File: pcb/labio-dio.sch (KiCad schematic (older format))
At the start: 98 parts

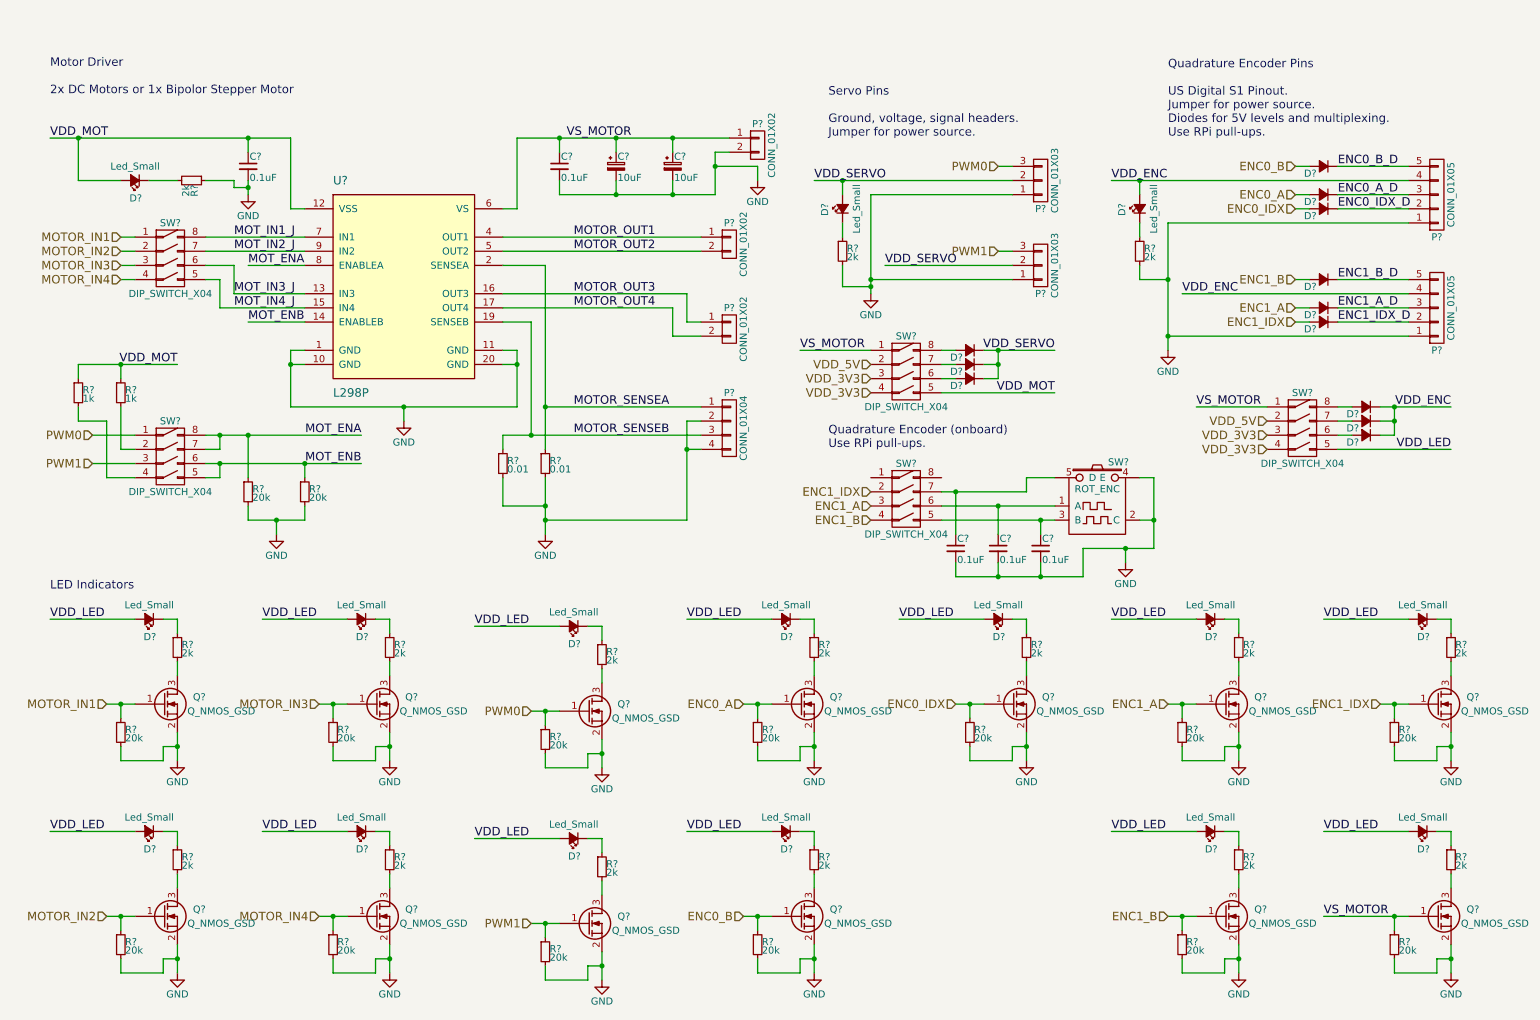
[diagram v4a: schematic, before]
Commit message: make extra footprints. start floorplan. fix display nets. add power expansion header.
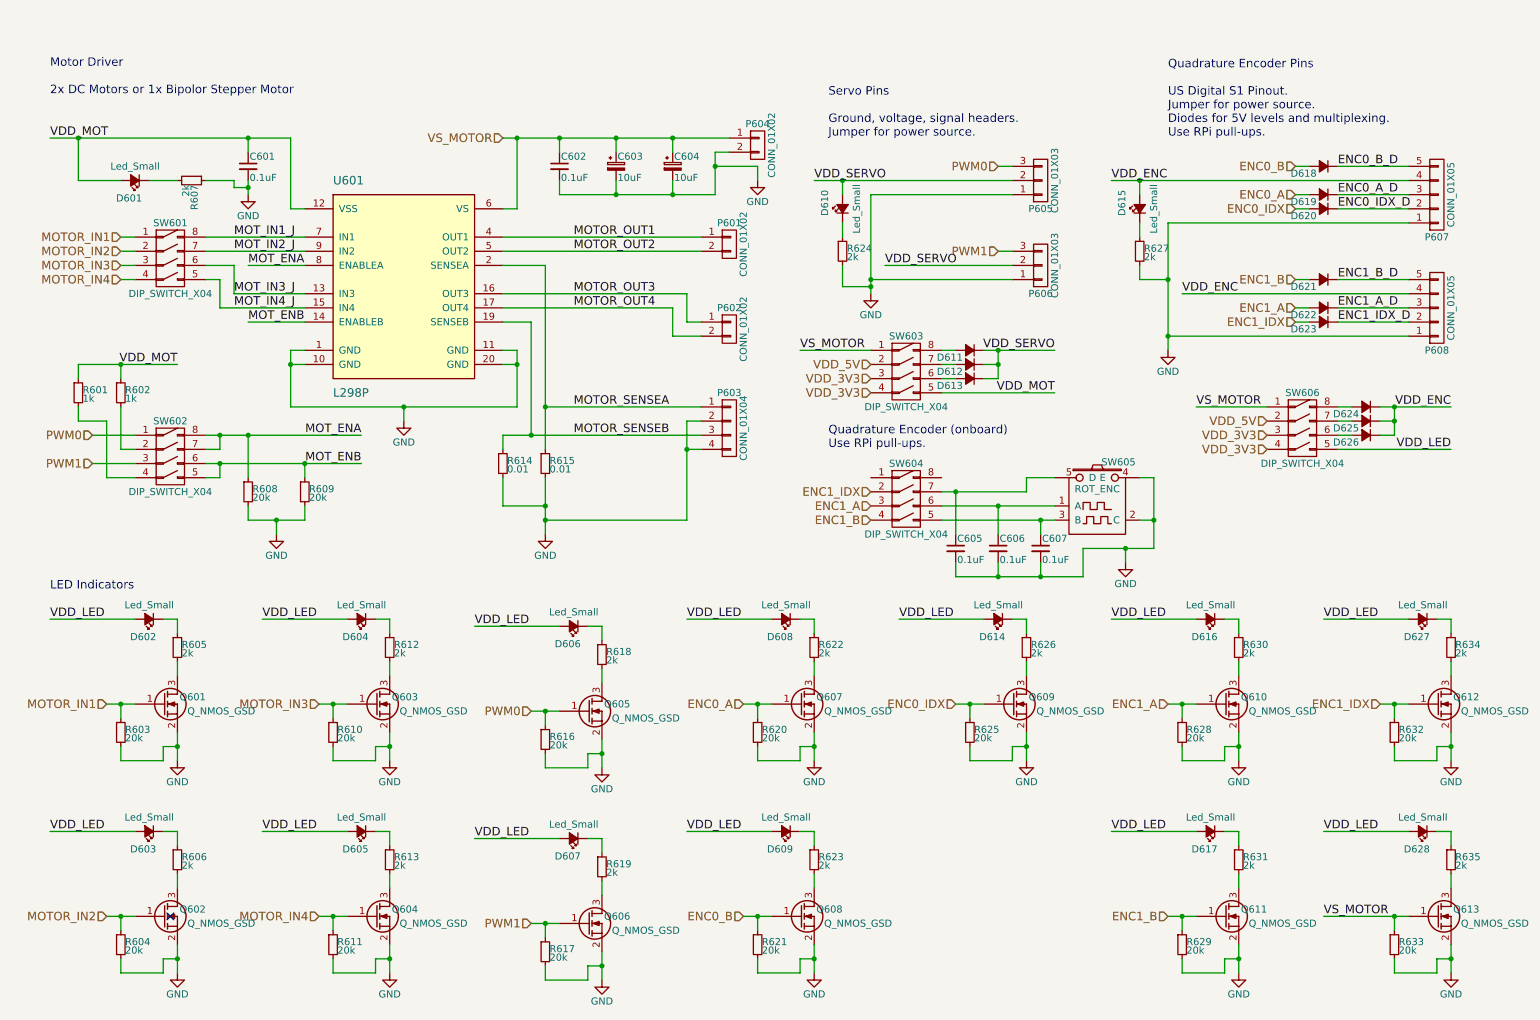
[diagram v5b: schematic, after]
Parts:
- C601, C602, C605, C606, C607: renamed from C?; footprint (none) -> Capacitors_SMD:C_0603
- C603, C604: renamed from C?; footprint (none) -> Capacitors_Tantalum_SMD:TantalC_SizeA_EIA-3216_Wave
- D601, D602, D603, D604, D605, D606, D607, D608, D609, D610, D614, D615, D616, D617, D627, D628: renamed from D?; footprint (none) -> LEDs:LED-0603
- D611, D612, D613, D618, D619, D620, D621, D622, D623, D624, D625, D626: renamed from D?; footprint (none) -> Diodes_SMD:SOD-523
- P601, P602, P604: renamed from P?; footprint (none) -> Pin_Headers:Pin_Header_Straight_1x02
- P603: renamed from P?; footprint (none) -> Pin_Headers:Pin_Header_Straight_1x04
- P605, P606: renamed from P?; footprint (none) -> Pin_Headers:Pin_Header_Straight_1x03
- P607, P608: renamed from P?; footprint (none) -> Pin_Headers:Pin_Header_Straight_1x05
- Q601, Q602, Q603, Q604, Q605, Q606, Q607, Q608, Q609, Q610, Q611, Q612, Q613: renamed from Q?; footprint (none) -> TO_SOT_Packages_SMD:SOT-23
- R601, R602, R603, R604, R605, R606, R607, R608, R609, R610, R611, R612, R613, R616, R617, R618, R619, R620, R621, R622, R623, R624, R625, R626, R627, R628, R629, R630, R631, R632, R633, R634, R635: renamed from R?; footprint (none) -> Resistors_SMD:R_0603
- R614, R615: renamed from R?; footprint (none) -> Resistors_SMD:R_1206
- SW601, SW602, SW603, SW604, SW606: renamed from SW?; footprint (none) -> labio-special:DIP-8_W7.62mm_SMT
- SW605: renamed from SW?; footprint (none) -> labio-special:Rot-Enc-12mm-Horiz-Button
- U601: renamed from U?; footprint (none) -> labio-special:PowerSO20
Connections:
- no-connect marks 0 -> 1

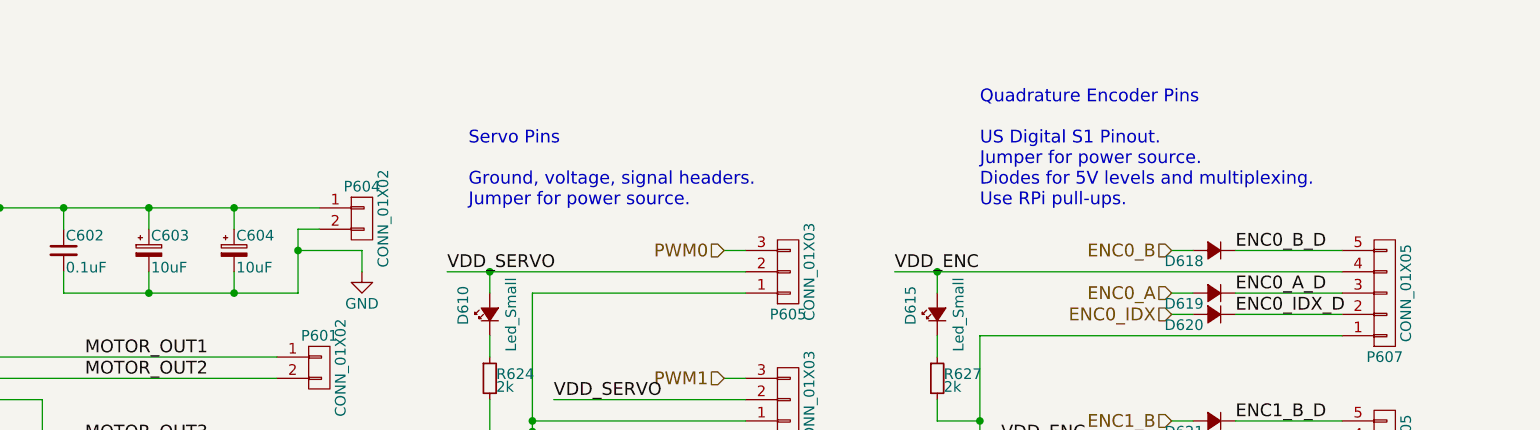
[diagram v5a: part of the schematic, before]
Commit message: floorplan on 150x85mm board, use al caps for motors
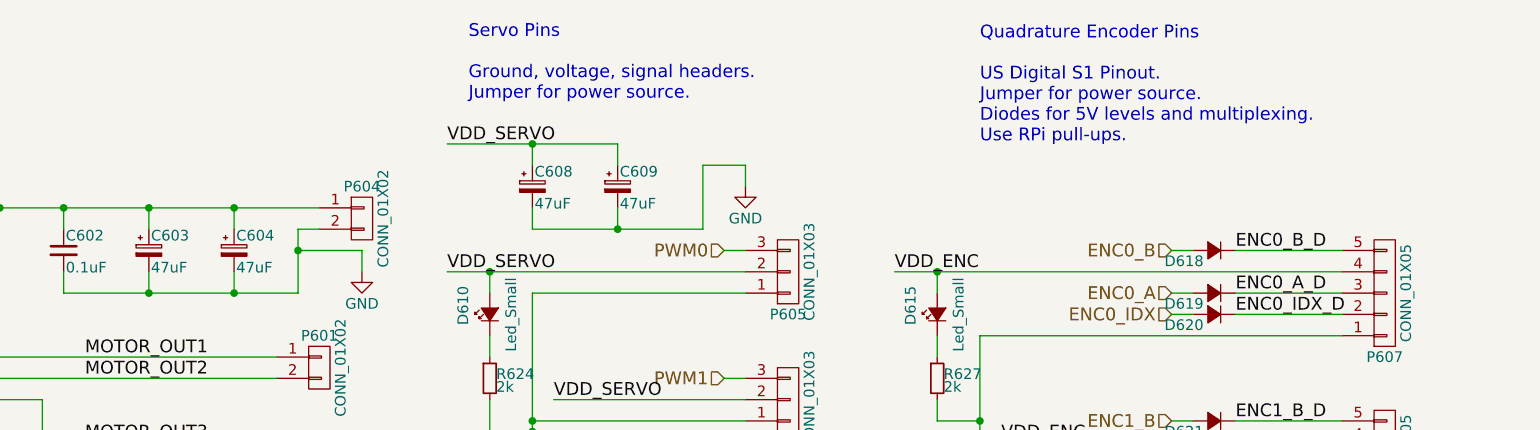
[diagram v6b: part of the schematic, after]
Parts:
- added C608, C609: 47uF, Capacitors_SMD:c_elec_6.3x5.8, symbol CP_Small
- C603, C604: value 10uF -> 47uF; footprint Capacitors_Tantalum_SMD:TantalC_SizeA_EIA-3216_Wave -> Capacitors_SMD:c_elec_6.3x5.8
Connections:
- net GND: now also C608.2, C609.2
- net VDD_SERVO: now also C608.1, C609.1
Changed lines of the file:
@@
 	1    0    0    1
 $EndComp
-Text Notes 8600 1500 0    60   ~ 0
+Text Notes 8600 1200 0    60   ~ 0
 Quadrature Encoder Pins\n\nUS Digital S1 Pinout.\nJumper for power source.\nDiodes for 5V levels and multiplexing.\nUse RPi pull-ups.
-Text Notes 6200 1500 0    60   ~ 0
+Text Notes 6200 1000 0    60   ~ 0
 Servo Pins\n\nGround, voltage, signal headers.\nJumper for power source.
 Text Notes 700  1200 0    60   ~ 0
@@
 P 4700 1700
 F 0 "C603" H 4710 1770 50  0000 L CNN
-F 1 "10uF" H 4710 1620 50  0000 L CNN
-F 2 "Capacitors_Tantalum_SMD:TantalC_SizeA_EIA-3216_Wave" H 4700 1700 50  0001 C CNN
+F 1 "47uF" H 4710 1620 50  0000 L CNN
+F 2 "Capacitors_SMD:c_elec_6.3x5.8" H 4700 1700 50  0001 C CNN
 F 3 "" H 4700 1700 50  0000 C CNN
 	1    4700 1700
@@
 P 5100 1700
 F 0 "C604" H 5110 1770 50  0000 L CNN
-F 1 "10uF" H 5110 1620 50  0000 L CNN
-F 2 "Capacitors_Tantalum_SMD:TantalC_SizeA_EIA-3216_Wave" H 5100 1700 50  0001 C CNN
+F 1 "47uF" H 5110 1620 50  0000 L CNN
+F 2 "Capacitors_SMD:c_elec_6.3x5.8" H 5100 1700 50  0001 C CNN
 F 3 "" H 5100 1700 50  0000 C CNN
 	1    5100 1700
@@
 VS_MOTOR
 Connection ~ 4000 1500
+$Comp
+L CP_Small C608
+U 1 1 577DDEB8
+P 6500 1400
+F 0 "C608" H 6510 1470 50  0000 L CNN
+F 1 "47uF" H 6510 1320 50  0000 L CNN
+F 2 "Capacitors_SMD:c_elec_6.3x5.8" H 6500 1400 50  0001 C CNN
+F 3 "" H 6500 1400 50  0000 C CNN
+	1    6500 1400
+	1    0    0    -1
+$EndComp
+$Comp
+L CP_Small C609
+U 1 1 577DE0C4
+P 6900 1400
+F 0 "C609" H 6910 1470 50  0000 L CNN
+F 1 "47uF" H 6910 1320 50  0000 L CNN
+F 2 "Capacitors_SMD:c_elec_6.3x5.8" H 6900 1400 50  0001 C CNN
+F 3 "" H 6900 1400 50  0000 C CNN
+	1    6900 1400
+	1    0    0    -1
+$EndComp
+Wire Wire Line
+	6100 1200 6900 1200
+Wire Wire Line
+	6500 1200 6500 1300
+Wire Wire Line
+	6900 1200 6900 1300
+Connection ~ 6500 1200
+$Comp
+L GND #PWR033
+U 1 1 577DE6E6
+P 7500 1400
+F 0 "#PWR033" H 7500 1150 50  0001 C CNN
+F 1 "GND" H 7500 1250 50  0000 C CNN
+F 2 "" H 7500 1400 50  0000 C CNN
+F 3 "" H 7500 1400 50  0000 C CNN
+	1    7500 1400
+	1    0    0    -1
+$EndComp
+Wire Wire Line
+	7500 1400 7500 1300
+Wire Wire Line
+	7500 1300 7300 1300
+Wire Wire Line
+	7300 1300 7300 1600
+Wire Wire Line
+	7300 1600 6500 1600
+Wire Wire Line
+	6900 1600 6900 1500
+Wire Wire Line
+	6500 1600 6500 1500
+Connection ~ 6900 1600
+Text Label 6100 1200 0    60   ~ 0
+VDD_SERVO
 $EndSCHEMATC

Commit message: update imu parts, adc rails, motor headers
* replace LSM303C accelerometer with LSM303D for better sensor ranges at same cost.
* add L3GD20H gyroscope so we have a 10-DOF imu. consider leaving depopulated for complexity.
* add 0 ohms to accel/gyro address and interrupt pins in case of later changes
* change ADC rails to 5V to read 5V power shunts. add level shifters to the 3.3V I2C bus.
* use 3.5mm pitch headers for motor terminal blocks to accept higher guage wire.

todo:
* redo ADC routing
* make space behind motor headers
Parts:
- P601, P602, P604: footprint Pin_Headers:Pin_Header_Straight_1x02 -> labio-special:Pin_Header_Straight_1x02_Pitch3.5mm
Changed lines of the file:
@@
 F 0 "P601" H 5500 2400 50  0000 C CNN
 F 1 "CONN_01X02" V 5600 2250 50  0000 C CNN
-F 2 "Pin_Headers:Pin_Header_Straight_1x02" H 5500 2250 50  0001 C CNN
+F 2 "labio-special:Pin_Header_Straight_1x02_Pitch3.5mm" H 5500 2250 50  0001 C CNN
 F 3 "" H 5500 2250 50  0000 C CNN
 	1    5500 2250
@@
 F 0 "P602" H 5500 3000 50  0000 C CNN
 F 1 "CONN_01X02" V 5600 2850 50  0000 C CNN
-F 2 "Pin_Headers:Pin_Header_Straight_1x02" H 5500 2850 50  0001 C CNN
+F 2 "labio-special:Pin_Header_Straight_1x02_Pitch3.5mm" H 5500 2850 50  0001 C CNN
 F 3 "" H 5500 2850 50  0000 C CNN
 	1    5500 2850
@@
 F 0 "P604" H 5700 1700 50  0000 C CNN
 F 1 "CONN_01X02" V 5800 1550 50  0000 C CNN
-F 2 "Pin_Headers:Pin_Header_Straight_1x02" H 5700 1550 50  0001 C CNN
+F 2 "labio-special:Pin_Header_Straight_1x02_Pitch3.5mm" H 5700 1550 50  0001 C CNN
 F 3 "" H 5700 1550 50  0000 C CNN
 	1    5700 1550
@@
 $EndComp
 $Comp
-L GND #PWR012
+L GND #PWR019
 U 1 1 575CE626
 P 5700 1800
-F 0 "#PWR012" H 5700 1550 50  0001 C CNN
+F 0 "#PWR019" H 5700 1550 50  0001 C CNN
 F 1 "GND" H 5700 1650 50  0000 C CNN
 F 2 "" H 5700 1800 50  0000 C CNN
@@
 $EndComp
 $Comp
-L GND #PWR013
+L GND #PWR020
 U 1 1 575CE734
 P 3200 3500
-F 0 "#PWR013" H 3200 3250 50  0001 C CNN
+F 0 "#PWR020" H 3200 3250 50  0001 C CNN
 F 1 "GND" H 3200 3350 50  0000 C CNN
 F 2 "" H 3200 3500 50  0000 C CNN
@@
 $EndComp
 $Comp
-L GND #PWR014
+L GND #PWR021
 U 1 1 575CE88B
 P 6500 2600
-F 0 "#PWR014" H 6500 2350 50  0001 C CNN
+F 0 "#PWR021" H 6500 2350 50  0001 C CNN
 F 1 "GND" H 6500 2450 50  0000 C CNN
 F 2 "" H 6500 2600 50  0000 C CNN
@@
 PWM0
 $Comp
-L GND #PWR015
+L GND #PWR022
 U 1 1 575D03C6
 P 8600 3000
-F 0 "#PWR015" H 8600 2750 50  0001 C CNN
+F 0 "#PWR022" H 8600 2750 50  0001 C CNN
 F 1 "GND" H 8600 2850 50  0000 C CNN
 F 2 "" H 8600 3000 50  0000 C CNN
@@
 $EndComp
 $Comp
-L GND #PWR016
+L GND #PWR023
 U 1 1 575D15A4
 P 2100 1900
-F 0 "#PWR016" H 2100 1650 50  0001 C CNN
+F 0 "#PWR023" H 2100 1650 50  0001 C CNN
 F 1 "GND" H 2100 1750 50  0000 C CNN
 F 2 "" H 2100 1900 50  0000 C CNN
@@
 $EndComp
 $Comp
-L GND #PWR017
+L GND #PWR024
 U 1 1 576DA4BF
 P 2300 4300
-F 0 "#PWR017" H 2300 4050 50  0001 C CNN
+F 0 "#PWR024" H 2300 4050 50  0001 C CNN
 F 1 "GND" H 2300 4150 50  0000 C CNN
 F 2 "" H 2300 4300 50  0000 C CNN
@@
 $EndComp
 $Comp
-L GND #PWR018
+L GND #PWR025
 U 1 1 576DC1F9
 P 4200 4300
-F 0 "#PWR018" H 4200 4050 50  0001 C CNN
+F 0 "#PWR025" H 4200 4050 50  0001 C CNN
 F 1 "GND" H 4200 4150 50  0000 C CNN
 F 2 "" H 4200 4300 50  0000 C CNN
@@
 $EndComp
 $Comp
-L GND #PWR019
+L GND #PWR026
 U 1 1 576E924C
 P 1600 5900
-F 0 "#PWR019" H 1600 5650 50  0001 C CNN
+F 0 "#PWR026" H 1600 5650 50  0001 C CNN
 F 1 "GND" H 1600 5750 50  0000 C CNN
 F 2 "" H 1600 5900 50  0000 C CNN
@@
 $EndComp
 $Comp
-L GND #PWR020
+L GND #PWR027
 U 1 1 576F45C1
 P 1600 7400
-F 0 "#PWR020" H 1600 7150 50  0001 C CNN
+F 0 "#PWR027" H 1600 7150 50  0001 C CNN
 F 1 "GND" H 1600 7250 50  0000 C CNN
 F 2 "" H 1600 7400 50  0000 C CNN
@@
 $EndComp
 $Comp
-L GND #PWR021
+L GND #PWR028
 U 1 1 576F87DD
 P 3100 5900
-F 0 "#PWR021" H 3100 5650 50  0001 C CNN
+F 0 "#PWR028" H 3100 5650 50  0001 C CNN
 F 1 "GND" H 3100 5750 50  0000 C CNN
 F 2 "" H 3100 5900 50  0000 C CNN
@@
 $EndComp
 $Comp
-L GND #PWR022
+L GND #PWR029
 U 1 1 576F8805
 P 3100 7400
-F 0 "#PWR022" H 3100 7150 50  0001 C CNN
+F 0 "#PWR029" H 3100 7150 50  0001 C CNN
 F 1 "GND" H 3100 7250 50  0000 C CNN
 F 2 "" H 3100 7400 50  0000 C CNN
@@
 $EndComp
 $Comp
-L GND #PWR023
+L GND #PWR030
 U 1 1 576F8970
 P 4600 5950
-F 0 "#PWR023" H 4600 5700 50  0001 C CNN
+F 0 "#PWR030" H 4600 5700 50  0001 C CNN
 F 1 "GND" H 4600 5800 50  0000 C CNN
 F 2 "" H 4600 5950 50  0000 C CNN
@@
 $EndComp
 $Comp
-L GND #PWR024
+L GND #PWR031
 U 1 1 576F8998
 P 4600 7450
-F 0 "#PWR024" H 4600 7200 50  0001 C CNN
+F 0 "#PWR031" H 4600 7200 50  0001 C CNN
 F 1 "GND" H 4600 7300 50  0000 C CNN
 F 2 "" H 4600 7450 50  0000 C CNN
@@
 $EndComp
 $Comp
-L GND #PWR025
+L GND #PWR032
 U 1 1 576F8F5D
 P 6100 5900
-F 0 "#PWR025" H 6100 5650 50  0001 C CNN
+F 0 "#PWR032" H 6100 5650 50  0001 C CNN
 F 1 "GND" H 6100 5750 50  0000 C CNN
 F 2 "" H 6100 5900 50  0000 C CNN
@@
 $EndComp
 $Comp
-L GND #PWR026
+L GND #PWR033
 U 1 1 576F8F85
 P 6100 7400
-F 0 "#PWR026" H 6100 7150 50  0001 C CNN
+F 0 "#PWR033" H 6100 7150 50  0001 C CNN
 F 1 "GND" H 6100 7250 50  0000 C CNN
 F 2 "" H 6100 7400 50  0000 C CNN
@@
 $EndComp
 $Comp
-L GND #PWR027
+L GND #PWR034
 U 1 1 576FAF5D
 P 7600 5900
-F 0 "#PWR027" H 7600 5650 50  0001 C CNN
+F 0 "#PWR034" H 7600 5650 50  0001 C CNN
 F 1 "GND" H 7600 5750 50  0000 C CNN
 F 2 "" H 7600 5900 50  0000 C CNN
@@
 $EndComp
 $Comp
-L GND #PWR028
+L GND #PWR035
 U 1 1 576FAF8A
 P 9100 5900
-F 0 "#PWR028" H 9100 5650 50  0001 C CNN
+F 0 "#PWR035" H 9100 5650 50  0001 C CNN
 F 1 "GND" H 9100 5750 50  0000 C CNN
 F 2 "" H 9100 5900 50  0000 C CNN
@@
 $EndComp
 $Comp
-L GND #PWR029
+L GND #PWR036
 U 1 1 576FAFB7
 P 10600 5900
-F 0 "#PWR029" H 10600 5650 50  0001 C CNN
+F 0 "#PWR036" H 10600 5650 50  0001 C CNN
 F 1 "GND" H 10600 5750 50  0000 C CNN
 F 2 "" H 10600 5900 50  0000 C CNN
@@
 $EndComp
 $Comp
-L GND #PWR030
+L GND #PWR037
 U 1 1 576FAFE4
 P 9100 7400
-F 0 "#PWR030" H 9100 7150 50  0001 C CNN
+F 0 "#PWR037" H 9100 7150 50  0001 C CNN
 F 1 "GND" H 9100 7250 50  0000 C CNN
 F 2 "" H 9100 7400 50  0000 C CNN
@@
 ENC1_IDX
 $Comp
-L GND #PWR031
+L GND #PWR038
 U 1 1 576FF975
 P 8300 4500
-F 0 "#PWR031" H 8300 4250 50  0001 C CNN
+F 0 "#PWR038" H 8300 4250 50  0001 C CNN
 F 1 "GND" H 8300 4350 50  0000 C CNN
 F 2 "" H 8300 4500 50  0000 C CNN
@@
 $EndComp
 $Comp
-L GND #PWR032
+L GND #PWR039
 U 1 1 57708A03
 P 10600 7400
-F 0 "#PWR032" H 10600 7150 50  0001 C CNN
+F 0 "#PWR039" H 10600 7150 50  0001 C CNN
 F 1 "GND" H 10600 7250 50  0000 C CNN
 F 2 "" H 10600 7400 50  0000 C CNN
@@
 Connection ~ 6500 1200
 $Comp
-L GND #PWR033
+L GND #PWR040
 U 1 1 577DE6E6
 P 7500 1400
-F 0 "#PWR033" H 7500 1150 50  0001 C CNN
+F 0 "#PWR040" H 7500 1150 50  0001 C CNN
 F 1 "GND" H 7500 1250 50  0000 C CNN
 F 2 "" H 7500 1400 50  0000 C CNN
